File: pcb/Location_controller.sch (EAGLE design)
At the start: 66 parts

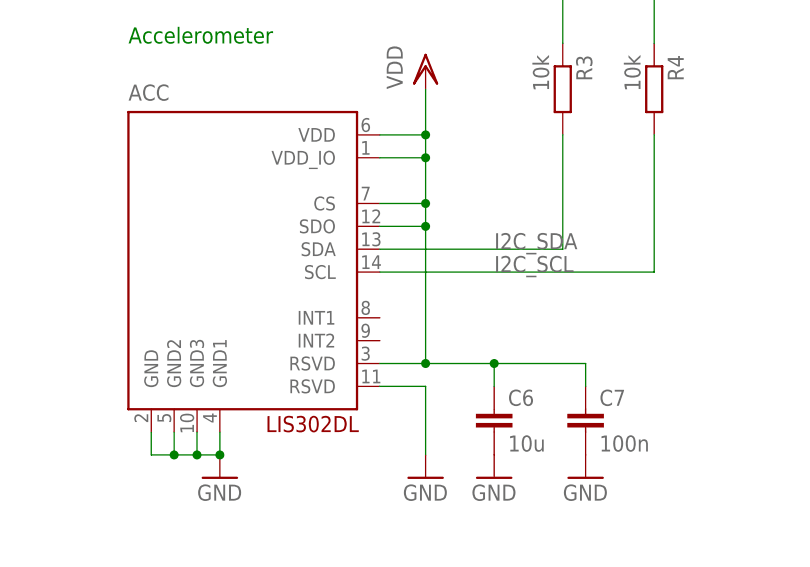
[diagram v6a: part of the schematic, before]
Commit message: Disconnect SDO pin on accelerometer
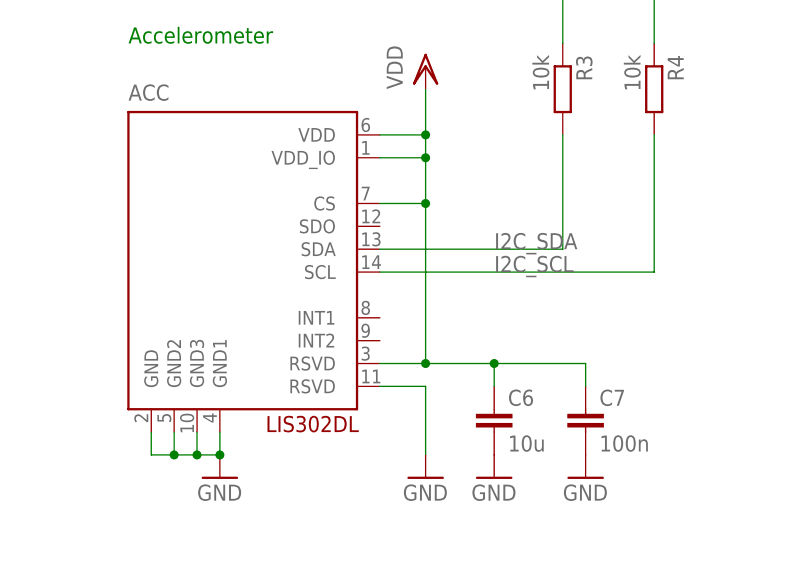
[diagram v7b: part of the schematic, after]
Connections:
- net VDD: no longer ACC.SDO
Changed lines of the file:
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@@
 <grid distance="0.1" unitdist="inch" unit="inch" style="lines" multiple="1" display="no" altdistance="0.01" altunitdist="inch" altunit="inch"/>
 <layers>
-<layer number="1" name="Top" color="4" fill="1" visible="yes" active="no"/>
-<layer number="16" name="Bottom" color="1" fill="1" visible="yes" active="no"/>
-<layer number="17" name="Pads" color="2" fill="1" visible="yes" active="no"/>
-<layer number="18" name="Vias" color="2" fill="1" visible="yes" active="no"/>
-<layer number="19" name="Unrouted" color="6" fill="1" visible="yes" active="no"/>
-<layer number="20" name="Dimension" color="15" fill="1" visible="yes" active="no"/>
-<layer number="21" name="tPlace" color="7" fill="1" visible="yes" active="no"/>
-<layer number="22" name="bPlace" color="7" fill="1" visible="yes" active="no"/>
-<layer number="23" name="tOrigins" color="15" fill="1" visible="yes" active="no"/>
-<layer number="24" name="bOrigins" color="15" fill="1" visible="yes" active="no"/>
-<layer number="25" name="tNames" color="7" fill="1" visible="yes" active="no"/>
-<layer number="26" name="bNames" color="7" fill="1" visible="yes" active="no"/>
-<layer number="27" name="tValues" color="7" fill="1" visible="yes" active="no"/>
-<layer number="28" name="bValues" color="7" fill="1" visible="yes" active="no"/>
+<layer number="1" name="Top" color="4" fill="1" visible="no" active="no"/>
+<layer number="16" name="Bottom" color="1" fill="1" visible="no" active="no"/>
+<layer number="17" name="Pads" color="2" fill="1" visible="no" active="no"/>
+<layer number="18" name="Vias" color="2" fill="1" visible="no" active="no"/>
+<layer number="19" name="Unrouted" color="6" fill="1" visible="no" active="no"/>
+<layer number="20" name="Dimension" color="15" fill="1" visible="no" active="no"/>
+<layer number="21" name="tPlace" color="7" fill="1" visible="no" active="no"/>
+<layer number="22" name="bPlace" color="7" fill="1" visible="no" active="no"/>
+<layer number="23" name="tOrigins" color="15" fill="1" visible="no" active="no"/>
+<layer number="24" name="bOrigins" color="15" fill="1" visible="no" active="no"/>
+<layer number="25" name="tNames" color="7" fill="1" visible="no" active="no"/>
+<layer number="26" name="bNames" color="7" fill="1" visible="no" active="no"/>
+<layer number="27" name="tValues" color="7" fill="1" visible="no" active="no"/>
+<layer number="28" name="bValues" color="7" fill="1" visible="no" active="no"/>
 <layer number="29" name="tStop" color="7" fill="3" visible="no" active="no"/>
 <layer number="30" name="bStop" color="7" fill="6" visible="no" active="no"/>
@@
 <layer number="35" name="tGlue" color="7" fill="4" visible="no" active="no"/>
 <layer number="36" name="bGlue" color="7" fill="5" visible="no" active="no"/>
-<layer number="37" name="tTest" color="7" fill="1" visible="yes" active="no"/>
-<layer number="38" name="bTest" color="7" fill="1" visible="yes" active="no"/>
+<layer number="37" name="tTest" color="7" fill="1" visible="no" active="no"/>
+<layer number="38" name="bTest" color="7" fill="1" visible="no" active="no"/>
 <layer number="39" name="tKeepout" color="4" fill="11" visible="no" active="no"/>
 <layer number="40" name="bKeepout" color="1" fill="11" visible="no" active="no"/>
@@
 <layer number="44" name="Drills" color="7" fill="1" visible="no" active="no"/>
 <layer number="45" name="Holes" color="7" fill="1" visible="no" active="no"/>
-<layer number="46" name="Milling" color="3" fill="1" visible="yes" active="no"/>
-<layer number="47" name="Measures" color="7" fill="1" visible="yes" active="no"/>
-<layer number="48" name="Document" color="7" fill="1" visible="yes" active="no"/>
-<layer number="49" name="Reference" color="7" fill="1" visible="yes" active="no"/>
-<layer number="50" name="dxf" color="7" fill="1" visible="yes" active="no"/>
-<layer number="51" name="tDocu" color="7" fill="1" visible="yes" active="no"/>
-<layer number="52" name="bDocu" color="7" fill="1" visible="yes" active="no"/>
-<layer number="53" name="tGND_GNDA" color="7" fill="9" visible="yes" active="no"/>
-<layer number="54" name="bGND_GNDA" color="1" fill="9" visible="yes" active="no"/>
-<layer number="56" name="wert" color="7" fill="1" visible="yes" active="no"/>
-<layer number="57" name="tCAD" color="10" fill="1" visible="yes" active="no"/>
-<layer number="58" name="bCAD" color="11" fill="1" visible="yes" active="no"/>
+<layer number="46" name="Milling" color="3" fill="1" visible="no" active="no"/>
+<layer number="47" name="Measures" color="7" fill="1" visible="no" active="no"/>
+<layer number="48" name="Document" color="7" fill="1" visible="no" active="no"/>
+<layer number="49" name="Reference" color="7" fill="1" visible="no" active="no"/>
+<layer number="50" name="dxf" color="7" fill="1" visible="no" active="no"/>
+<layer number="51" name="tDocu" color="7" fill="1" visible="no" active="no"/>
+<layer number="52" name="bDocu" color="7" fill="1" visible="no" active="no"/>
+<layer number="53" name="tGND_GNDA" color="7" fill="9" visible="no" active="no"/>
+<layer number="54" name="bGND_GNDA" color="1" fill="9" visible="no" active="no"/>
+<layer number="56" name="wert" color="7" fill="1" visible="no" active="no"/>
+<layer number="57" name="tCAD" color="10" fill="1" visible="no" active="no"/>
+<layer number="58" name="bCAD" color="11" fill="1" visible="no" active="no"/>
 <layer number="91" name="Nets" color="2" fill="1" visible="yes" active="yes"/>
 <layer number="92" name="Busses" color="1" fill="1" visible="yes" active="yes"/>
@@
 <pinref part="ACC" gate="G$1" pin="RSVD@1"/>
 <wire x1="-43.18" y1="0" x2="-38.1" y2="0" width="0.1524" layer="91"/>
-<wire x1="-38.1" y1="0" x2="-38.1" y2="15.24" width="0.1524" layer="91"/>
+<wire x1="-38.1" y1="0" x2="-38.1" y2="17.78" width="0.1524" layer="91"/>
 <junction x="-38.1" y="22.86"/>
 <pinref part="ACC" gate="G$1" pin="CS"/>
-<wire x1="-38.1" y1="15.24" x2="-38.1" y2="17.78" width="0.1524" layer="91"/>
 <wire x1="-38.1" y1="17.78" x2="-38.1" y2="22.86" width="0.1524" layer="91"/>
 <wire x1="-43.18" y1="17.78" x2="-38.1" y2="17.78" width="0.1524" layer="91"/>
@@
 <wire x1="-20.32" y1="0" x2="-20.32" y2="-2.54" width="0.1524" layer="91"/>
 <junction x="-30.48" y="0"/>
-<pinref part="ACC" gate="G$1" pin="SDO"/>
-<wire x1="-43.18" y1="15.24" x2="-38.1" y2="15.24" width="0.1524" layer="91"/>
-<junction x="-38.1" y="15.24"/>
-</segment>
-<segment>
+</segment>
+<segment>

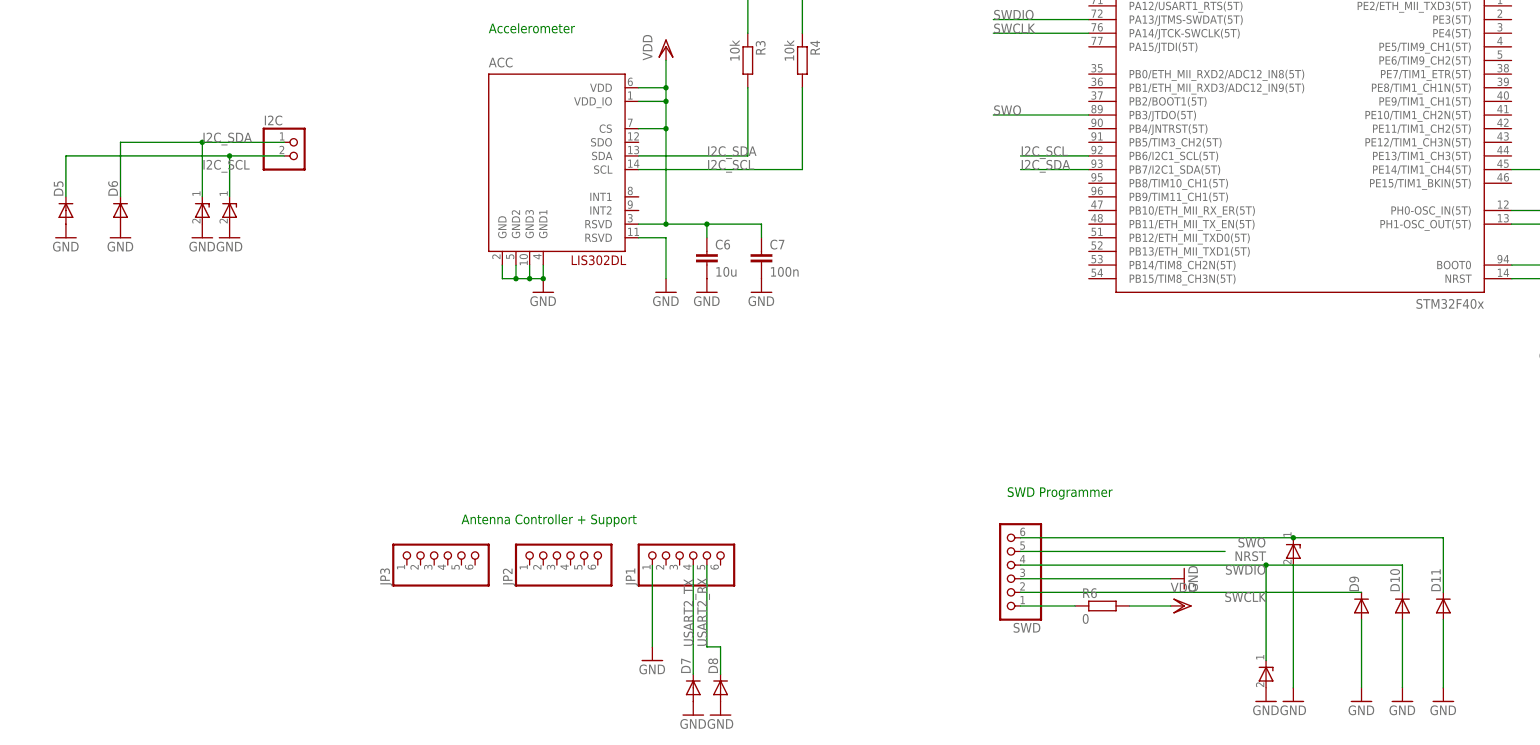
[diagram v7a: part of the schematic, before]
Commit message: Add solder bridges to disconnect accelerometer
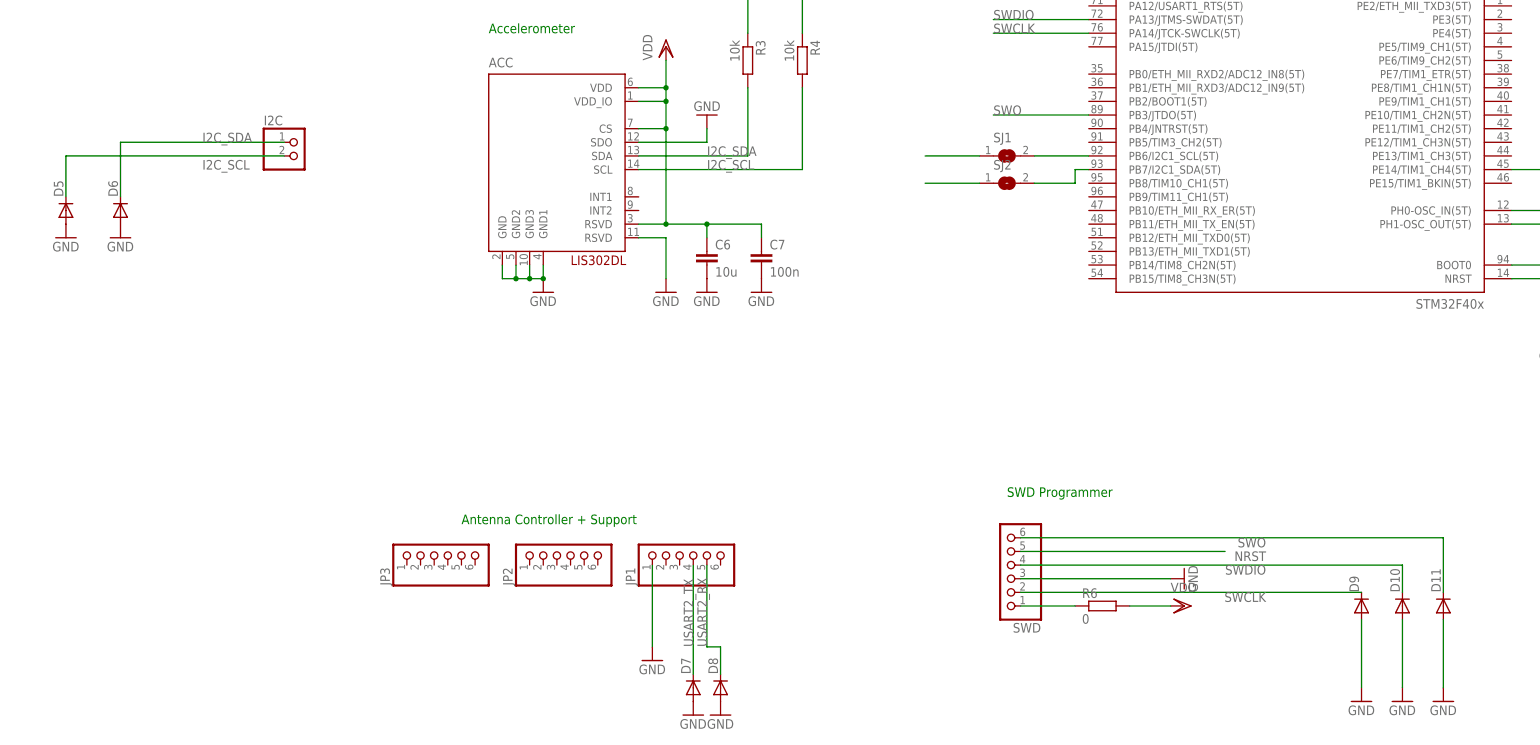
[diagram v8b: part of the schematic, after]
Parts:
- removed D1, D2, D3, D4: ZDIODE, stm32f4:ZDIODE
- added SJ1, SJ2: (no value), jumper:SJ
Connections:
- new net N$18: SJ2.2, STM32F4.PB7/I2C1_SDA(5T)
- new net N$20: SJ1.2, STM32F4.PB6/I2C1_SCL(5T)
- net GND: now also ACC.SDO; no longer D1.P2, D2.P2, D3.P2, D4.P2
- net I2C_SCL: now also SJ1.1; no longer D2.P1, STM32F4.PB6/I2C1_SCL(5T)
- net I2C_SDA: now also SJ2.1; no longer D1.P1, STM32F4.PB7/I2C1_SDA(5T)
- net SWDIO: no longer D4.P1
- net SWO: no longer D3.P1
